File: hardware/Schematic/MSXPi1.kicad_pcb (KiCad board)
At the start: 2 copper layers, 102.6 x 65.3 mm, 48 parts, among them J1 Raspberry_Pi_Zero_2_3, J2 JTAG, J3 Conn_02x07_Odd_Even, J4 Conn_02x06_Odd_Even, J5 SJ-2509N, P1 MSX_CONNECTOR, U1 EPM3064ALC44-10

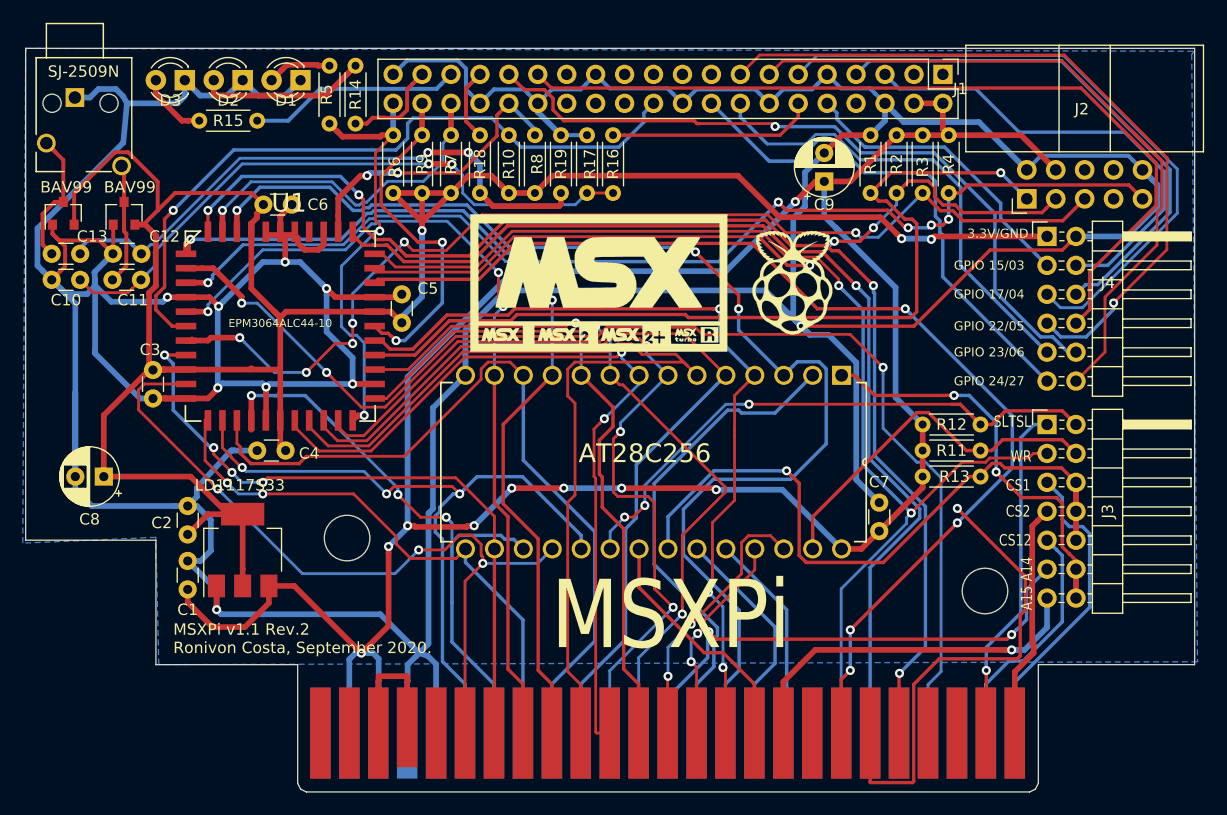
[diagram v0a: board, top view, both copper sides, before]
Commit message: PCB v1.1 Rev.3 - Replaced CPLD by TQFP package (epm3064atc44-10n).
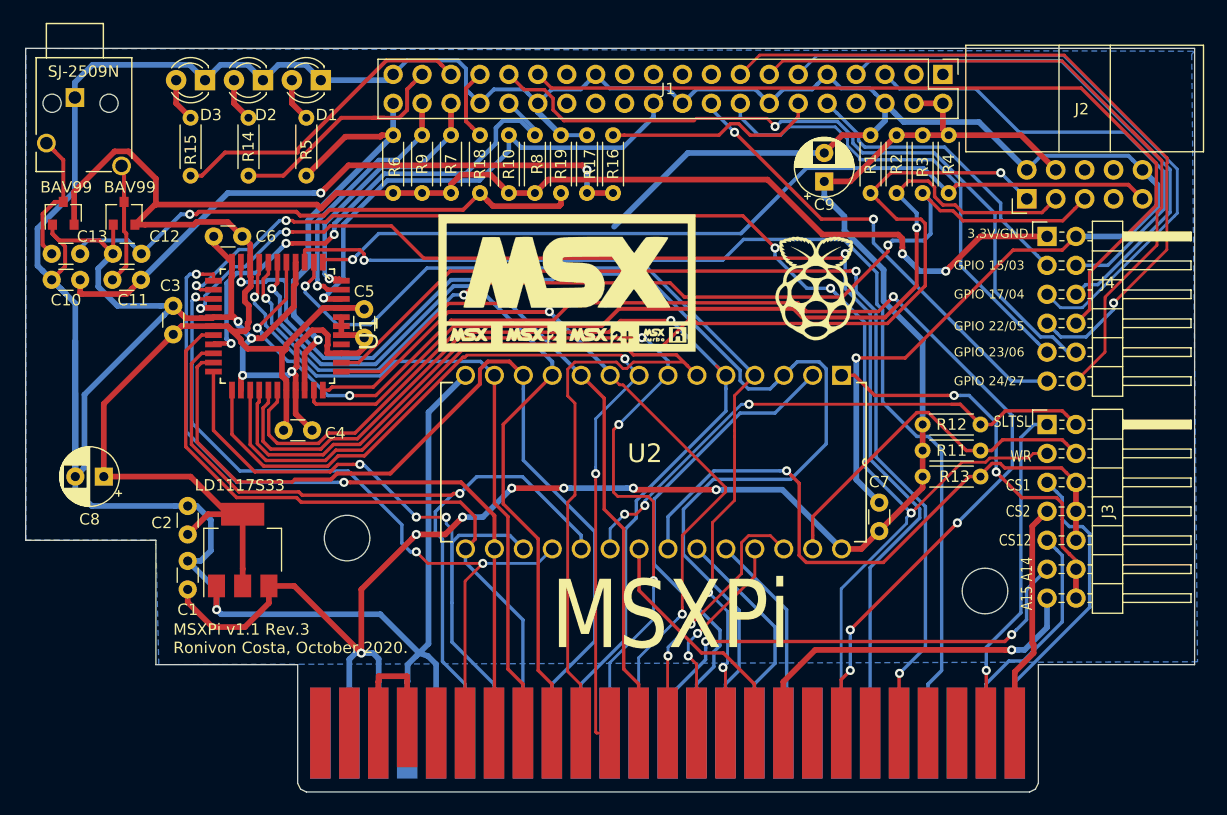
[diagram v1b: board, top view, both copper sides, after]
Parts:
- J1: value Raspberry_Pi_Zero_2_3 -> J1 - Raspberry_Pi_Zero_2_3
- U1: value EPM3064ALC44-10 -> EPM3064ATC44-10N; footprint MyFootprints:PLCC127P1765X1765X457-44N -> MyFootprints:QFP80P1200X1200X120-44N
- moved R14 10.5 mm to (114.3, 73.7)
- moved C3 8.32 mm to (107.7, 90.2), turned to 270 degrees
- moved C6 7.41 mm to (111.3, 84.1), turned to 0 degrees
- moved C4 5.14 mm to (119.9, 101.1), turned to 180 degrees
- moved C5 5.04 mm to (124.5, 93.0), turned to 90 degrees
- moved R5 5.00 mm to (119.4, 73.7)
- moved G*** 2.79 mm to (142.2, 88.1)
- moved G*** 2.09 mm to (164.1, 88.6)
- moved D1 1.78 mm to (120.7, 70.4)
- moved D2 1.78 mm to (115.6, 70.4)
- moved D3 1.78 mm to (110.5, 70.4)
- moved R15 0.80 mm to (109.2, 73.7), turned to 270 degrees
- moved U1 0.25 mm to (116.8, 91.9), turned to 270 degrees
- renumbered AT28C256 to U2
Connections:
- J1 pad 1: Net-(J1-Pad1) -> (no net)
- J1 pad 17: Net-(J1-Pad17) -> (no net)
- J1 pad 19: Net-(J1-Pad19) -> (no net)
- J1 pad 21: Net-(J1-Pad21) -> (no net)
- J1 pad 23: Net-(J1-Pad23) -> (no net)
- J1 pad 24: Net-(J1-Pad24) -> (no net)
- J1 pad 26: Net-(J1-Pad26) -> (no net)
- J1 pad 27: Net-(J1-Pad27) -> (no net)
- J1 pad 28: Net-(J1-Pad28) -> (no net)
- J1 pad 3: Net-(J1-Pad3) -> (no net)
- J1 pad 8: Net-(J1-Pad8) -> (no net)
- J2 pad 6: Net-(J2-Pad6) -> (no net)
- J2 pad 7: Net-(J2-Pad7) -> (no net)
- J2 pad 8: Net-(J2-Pad8) -> (no net)
- P1 pad 12: Net-(P1-Pad12) -> (no net)
- P1 pad 15: Net-(P1-Pad15) -> (no net)
- P1 pad 16: Net-(P1-Pad16) -> (no net)
- P1 pad 42: Net-(P1-Pad42) -> (no net)
- P1 pad 48: Net-(P1-Pad48) -> (no net)
- P1 pad 49: Net-(P1-Pad49) -> (no net)
- P1 pad 5: Net-(P1-Pad5) -> (no net)
- P1 pad 50: Net-(P1-Pad50) -> (no net)
- P1 pad 6: Net-(P1-Pad6) -> (no net)
- P1 pad 8: Net-(P1-Pad8) -> (no net)
- P1 pad 9: Net-(P1-Pad9) -> (no net)
- U1 pad 1: GNDREF -> TDI
- U1 pad 10: GNDREF -> A7
- U1 pad 11: D2 -> GNDREF
- U1 pad 12: SPI_RDY -> D4
- U1 pad 13: TMS -> WR
- U1 pad 14: D4 -> D6
- U1 pad 15: +3V3 -> IORQ
- U1 pad 16: D6 -> GNDREF
- U1 pad 17: GNDREF -> +3V3
- U1 pad 19: D7 -> SPI_MISO
- U1 pad 2: GNDREF -> A6
- U1 pad 20: D1 -> D7
- U1 pad 21: D5 -> D1
- U1 pad 22: GNDREF -> D5
- U1 pad 23: +3V3 -> A2
- U1 pad 24: A2 -> GNDREF
- U1 pad 26: A3 -> TCK
- U1 pad 27: A5 -> A3
- U1 pad 28: SPI_CS -> A5
- U1 pad 29: A1 -> +3V3
- U1 pad 3: +3V3 -> WAIT
- U1 pad 31: A0 -> SPI_CS
- U1 pad 32: TCK -> TDO
- U1 pad 33: A6 -> A1
- U1 pad 34: SPI_SCLK -> A0
- U1 pad 35: +3V3 -> BUSDIR
- U1 pad 37: RD -> (no net)
- U1 pad 38: TDO -> GNDREF
- U1 pad 39: WR -> GNDREF
- U1 pad 4: A7 -> GNDREF
- U1 pad 40: IORQ -> GNDREF
- U1 pad 41: SPI_MISO -> +3V3
- U1 pad 42: GNDREF -> SPI_RDY
- U1 pad 43: Net-(U1-Pad43) -> SPI_SCLK
- U1 pad 44: GNDREF -> SPI_MOSI
- U1 pad 5: SPI_MOSI -> RD
- U1 pad 6: BUSDIR -> D0
- U1 pad 7: TDI -> TMS
- U1 pad 8: WAIT -> D2
- U1 pad 9: D0 -> +3V3
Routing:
- net +5V: track 218.2 -> 160.1 mm, vias 9 -> 7
- net GNDREF: track 492.9 -> 440.3 mm, vias 9 -> 6
- net Net-(P1-Pad12): track 42.7 -> 0.00 mm, vias 1 -> 0
- net RD: track 98.0 -> 118.5 mm, vias 4 -> 6
- net TCK: track 78.0 -> 97.8 mm
- net BUSDIR: track 112.1 -> 92.6 mm, vias 4 -> 2
- net SPI_RDY: track 62.3 -> 42.8 mm
- net TDI: track 95.7 -> 77.1 mm, vias 5 -> 1
- net +3V3: track 212.0 -> 193.4 mm, vias 3 -> 2
- net WR: track 103.7 -> 121.7 mm, vias 2 -> 5
- net IORQ: track 92.0 -> 109.1 mm, vias 1 -> 3
- net TDO: track 68.3 -> 84.4 mm, vias 3 -> 1
- net SPI_MISO: track 30.5 -> 45.9 mm, vias 2 -> 3
- net D2: track 74.9 -> 61.5 mm, vias 3 -> 1
- net A5: track 77.1 -> 89.0 mm, vias 0 -> 1
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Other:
- board text added: "MSXPi v1.1 Rev.3 Ronivon Costa, October 2020."
- board text removed: "MSXPi v1.1 Rev.2 Ronivon Costa, September 2020."
